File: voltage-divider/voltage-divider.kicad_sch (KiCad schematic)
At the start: 0 parts

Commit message: Schematic is passing ERC
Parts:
- added BT1: 9, symbol Device:Battery
- added R1: 4k, symbol Device:R_US
- added R2: 5k, symbol Device:R_US
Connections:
- new net +9V: BT1.1 (+), R1.1
- new net GND: BT1.2 (-), R2.2
- new net Vin: R1.2, R2.1

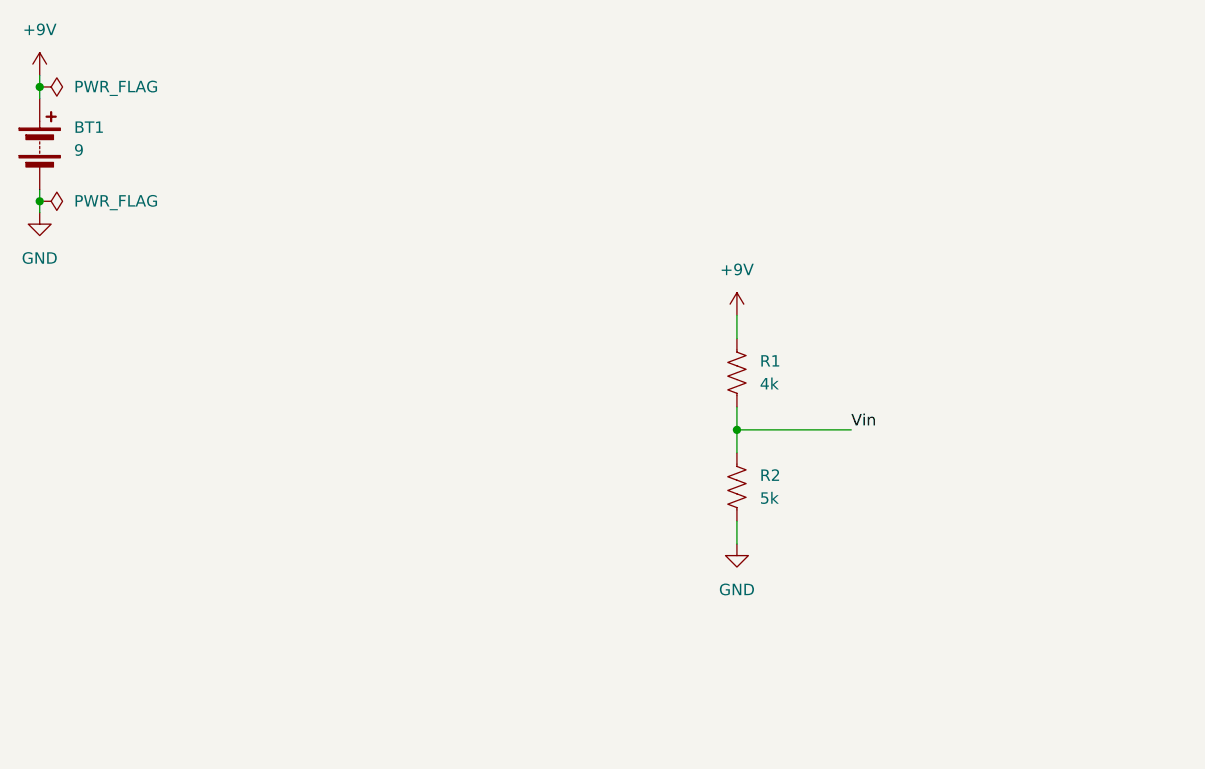
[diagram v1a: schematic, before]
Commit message: Added metadata to schematic
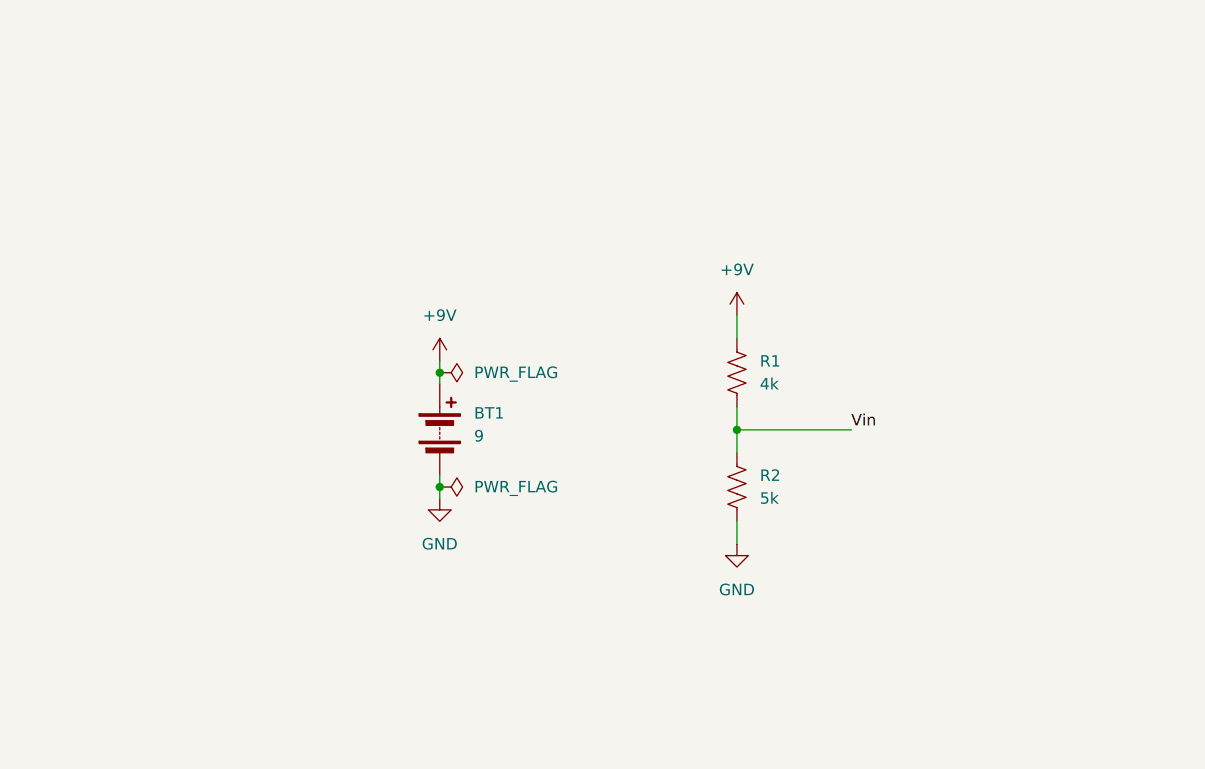
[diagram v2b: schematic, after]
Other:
- company: (none) -> Duke
- title: (none) -> KiCAD/SPICE Lab
- moved on the sheet: BT1
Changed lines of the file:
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@@
 	(paper "A4")
 	(title_block
+		(title "KiCAD/SPICE Lab")
 		(rev "v1.0.0")
+		(company "Duke")
 	)
 	(junction
-		(at 24.13 38.1)
+		(at 68.58 69.85)
 		(diameter 0)
 		(color 0 0 0 0)
@@
 	)
 	(junction
-		(at 24.13 25.4)
+		(at 68.58 57.15)
 		(diameter 0)
 		(color 0 0 0 0)
@@
 	(wire
 		(pts
-			(xy 24.13 36.83) (xy 24.13 38.1)
-		)
-		(stroke
-			(width 0)
-			(type default)
-		)
-	)
-	(wire
-		(pts
-			(xy 24.13 24.13) (xy 24.13 25.4)
+			(xy 68.58 68.58) (xy 68.58 69.85)
+		)
+		(stroke
+			(width 0)
+			(type default)
+		)
+	)
+	(wire
+		(pts
+			(xy 68.58 55.88) (xy 68.58 57.15)
 		)
 		(stroke
@@
 	(wire
 		(pts
-			(xy 24.13 25.4) (xy 24.13 26.67)
-		)
-		(stroke
-			(width 0)
-			(type default)
-		)
-	)
-	(wire
-		(pts
-			(xy 24.13 38.1) (xy 24.13 39.37)
+			(xy 68.58 57.15) (xy 68.58 58.42)
+		)
+		(stroke
+			(width 0)
+			(type default)
+		)
+	)
+	(wire
+		(pts
+			(xy 68.58 69.85) (xy 68.58 71.12)
 		)
 		(stroke
@@
 	(symbol
 		(lib_id "power:+9V")
-		(at 24.13 24.13 0)
+		(at 68.58 55.88 0)
 		(unit 1)
 		(exclude_from_sim no)
@@
 		(fields_autoplaced yes)
 		(property "Reference" "#PWR01"
-			(at 24.13 27.94 0)
+			(at 68.58 59.69 0)
 			(effects
 				(font
@@
 		)
 		(property "Value" "+9V"
-			(at 24.13 19.05 0)
-			(effects
-				(font
-					(size 1.27 1.27)
-				)
-			)
-		)
-		(property "Footprint" ""
-			(at 24.13 24.13 0)
+			(at 68.58 50.8 0)
+			(effects
+				(font
+					(size 1.27 1.27)
+				)
+			)
+		)
+		(property "Footprint" ""
+			(at 68.58 55.88 0)
 			(effects
 				(font
@@
 		)
 		(property "Datasheet" ""
-			(at 24.13 24.13 0)
+			(at 68.58 55.88 0)
 			(effects
 				(font
@@
 		)
 		(property "Description" "Power symbol creates a global label with name \"+9V\""
-			(at 24.13 24.13 0)
+			(at 68.58 55.88 0)
 			(effects
 				(font
@@
 	(symbol
 		(lib_id "Device:Battery")
-		(at 24.13 31.75 0)
+		(at 68.58 63.5 0)
 		(unit 1)
 		(exclude_from_sim no)
@@
 		(fields_autoplaced yes)
 		(property "Reference" "BT1"
-			(at 27.94 29.9084 0)
+			(at 72.39 61.6584 0)
 			(effects
 				(font
@@
 		)
 		(property "Value" "9"
-			(at 27.94 32.4484 0)
+			(at 72.39 64.1984 0)
 			(effects
 				(font
@@
 		)
 		(property "Footprint" ""
-			(at 24.13 30.226 90)
+			(at 68.58 61.976 90)
 			(effects
 				(font
@@
 		)
 		(property "Datasheet" "~"
-			(at 24.13 30.226 90)
+			(at 68.58 61.976 90)
 			(effects
 				(font
@@
 		)
 		(property "Description" "Multiple-cell battery"
-			(at 24.13 31.75 0)
+			(at 68.58 63.5 0)
 			(effects
 				(font
@@
 		)
 		(property "Sim.Device" "V"
-			(at 24.13 31.75 0)
+			(at 68.58 63.5 0)
 			(effects
 				(font
@@
 		)
 		(property "Sim.Type" "DC"
-			(at 24.13 31.75 0)
+			(at 68.58 63.5 0)
 			(effects
 				(font
@@
 		)
 		(property "Sim.Pins" "1=+ 2=-"
-			(at 24.13 31.75 0)
+			(at 68.58 63.5 0)
 			(effects
 				(font
@@
 	(symbol
 		(lib_id "power:PWR_FLAG")
-		(at 24.13 38.1 270)
+		(at 68.58 69.85 270)
 		(unit 1)
 		(exclude_from_sim no)
@@
 		(fields_autoplaced yes)
 		(property "Reference" "#FLG02"
-			(at 26.035 38.1 0)
+			(at 70.485 69.85 0)
 			(effects
 				(font
@@
 		)
 		(property "Value" "PWR_FLAG"
-			(at 27.94 38.0999 90)
+			(at 72.39 69.8499 90)
 			(effects
 				(font
@@
 		)
 		(property "Footprint" ""
-			(at 24.13 38.1 0)
+			(at 68.58 69.85 0)
 			(effects
 				(font
@@
 		)
 		(property "Datasheet" "~"
-			(at 24.13 38.1 0)
+			(at 68.58 69.85 0)
 			(effects
 				(font
@@
 		)
 		(property "Description" "Special symbol for telling ERC where power comes from"
-			(at 24.13 38.1 0)
+			(at 68.58 69.85 0)
 			(effects
 				(font
@@
 	(symbol
 		(lib_id "power:GND")
-		(at 24.13 39.37 0)
+		(at 68.58 71.12 0)
 		(unit 1)
 		(exclude_from_sim no)
@@
 		(fields_autoplaced yes)
 		(property "Reference" "#PWR02"
-			(at 24.13 45.72 0)
+			(at 68.58 77.47 0)
 			(effects
 				(font
@@
 		)
 		(property "Value" "GND"
-			(at 24.13 44.45 0)
-			(effects
-				(font
-					(size 1.27 1.27)
-				)
-			)
-		)
-		(property "Footprint" ""
-			(at 24.13 39.37 0)
+			(at 68.58 76.2 0)
+			(effects
+				(font
+					(size 1.27 1.27)
+				)
+			)
+		)
+		(property "Footprint" ""
+			(at 68.58 71.12 0)
 			(effects
 				(font
@@
 		)
 		(property "Datasheet" ""
-			(at 24.13 39.37 0)
+			(at 68.58 71.12 0)
 			(effects
 				(font
@@
 		)
 		(property "Description" "Power symbol creates a global label with name \"GND\" , ground"
-			(at 24.13 39.37 0)
+			(at 68.58 71.12 0)
 			(effects
 				(font
@@
 	(symbol
 		(lib_id "power:PWR_FLAG")
-		(at 24.13 25.4 270)
+		(at 68.58 57.15 270)
 		(unit 1)
 		(exclude_from_sim no)
@@
 		(fields_autoplaced yes)
 		(property "Reference" "#FLG01"
-			(at 26.035 25.4 0)
+			(at 70.485 57.15 0)
 			(effects
 				(font
@@
 		)
 		(property "Value" "PWR_FLAG"
-			(at 27.94 25.3999 90)
+			(at 72.39 57.1499 90)
 			(effects
 				(font
@@
 		)
 		(property "Footprint" ""
-			(at 24.13 25.4 0)
+			(at 68.58 57.15 0)
 			(effects
 				(font
@@
 		)
 		(property "Datasheet" "~"
-			(at 24.13 25.4 0)
+			(at 68.58 57.15 0)
 			(effects
 				(font
@@
 		)
 		(property "Description" "Special symbol for telling ERC where power comes from"
-			(at 24.13 25.4 0)
-			(effects
-				(font
+			(at 68.58 57.15 0)
+			(effects
+				(font

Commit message: Updated schematic to include potentiometer and created PCB layout
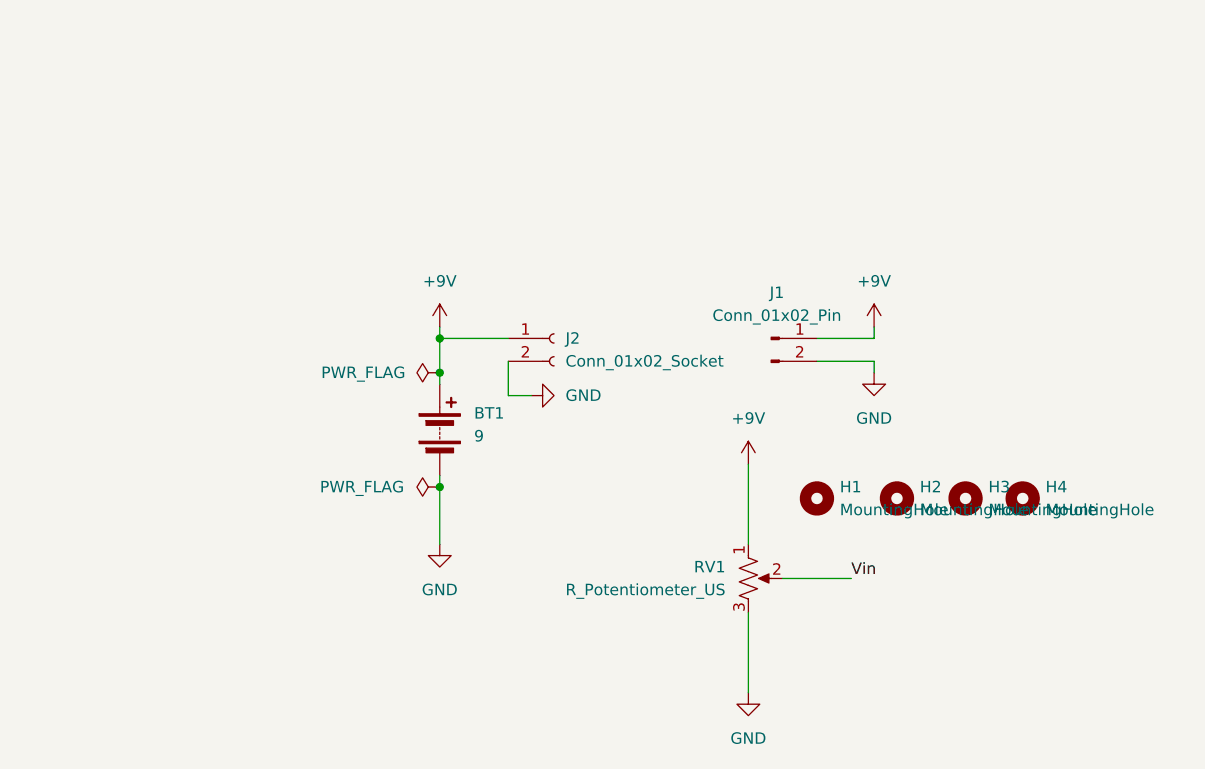
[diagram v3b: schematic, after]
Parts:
- removed R1: 4k, symbol Device:R_US
- removed R2: 5k, symbol Device:R_US
- added H1, H2, H3, H4: MountingHole, MountingHole:MountingHole_3.2mm_M3, symbol Mechanical:MountingHole
- added J1: Conn_01x02_Pin, Connector_JST:JST_XA_B02B-XASK-1-A_1x02_P2.50mm_Vertical, symbol Connector:Conn_01x02_Pin
- added J2: Conn_01x02_Socket, Connector_JST:JST_XA_B02B-XASK-1-A_1x02_P2.50mm_Vertical, symbol Connector:Conn_01x02_Socket
- added RV1: R_Potentiometer_US, Potentiometer_THT:Potentiometer_Alpha_RD901F-40-00D_Single_Vertical, symbol Device:R_Potentiometer_US
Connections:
- net +9V: now also J1.1 (Pin_1), J2.1 (Pin_1), RV1.1
- net GND: now also J1.2 (Pin_2), J2.2 (Pin_2), RV1.3
- net Vin: now also RV1.2
